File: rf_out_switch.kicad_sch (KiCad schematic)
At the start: 11 parts, among them P15 CONUFL001-SMD-T, P16 CONUFL001-SMD-T, U33 QPC1022TR7, U34 QPC1022TR7

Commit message: Lots of little cleanups
Signed-off-by: Corey Minyard <corey@minyard.net>
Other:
- note added: "Remove this resistor to disable all RF switches, then the zero-ohms connecting TX and RX directly to the antennas can be installed."
- note added: "This RF switch setup handles TX active/standby. On board 1 the zero ohm resistor is not populated. On board 2 or on simplex boards none of the switch circuitry is populated (or the resistor to the left is removed to disable the switches) and only the zero ohm resistor is populated."
- note removed: "This RF switch setup handles TX active/standby. On board 1 the zero ohm resistor is not populated. On board 2 or on simplex boards none of the switch circuitry is populated and only the zero ohm resistor is populated."
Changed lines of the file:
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@@
 		)
 	)
-	(text "This RF switch setup handles TX active/standby.\nOn board 1 the zero ohm resistor is not populated.  On board 2\nor on simplex boards none of the switch circuitry is\npopulated and only the zero ohm resistor is populated."
+	(text "This RF switch setup handles TX active/standby.\nOn board 1 the zero ohm resistor is not populated.  On board 2\nor on simplex boards none of the switch circuitry is\npopulated (or the resistor to the left is removed to disable\nthe switches) and only the zero ohm resistor is populated."
 		(exclude_from_sim no)
 		(at 156.21 147.32 0)
 		(effects
 			(font
+				(size 1.524 1.524)
+			)
+		)
+	)
+	(text "Remove this resistor to disable all RF switches,\nthen the zero-ohms connecting TX and RX directly\nto the antennas can be installed."
+		(exclude_from_sim no)
+		(at 53.848 125.222 0)
+		(effects
+			(font
+				(size 1.524 1.524)
+			)
+		)
+	)
+	(text "Remove this resistor to disable all RF switches,\nthen the zero-ohms connecting TX and RX directly\nto the antennas can be installed."
+		(exclude_from_sim no)
+		(at 53.086 125.222 0)
+		(effects
+			(font

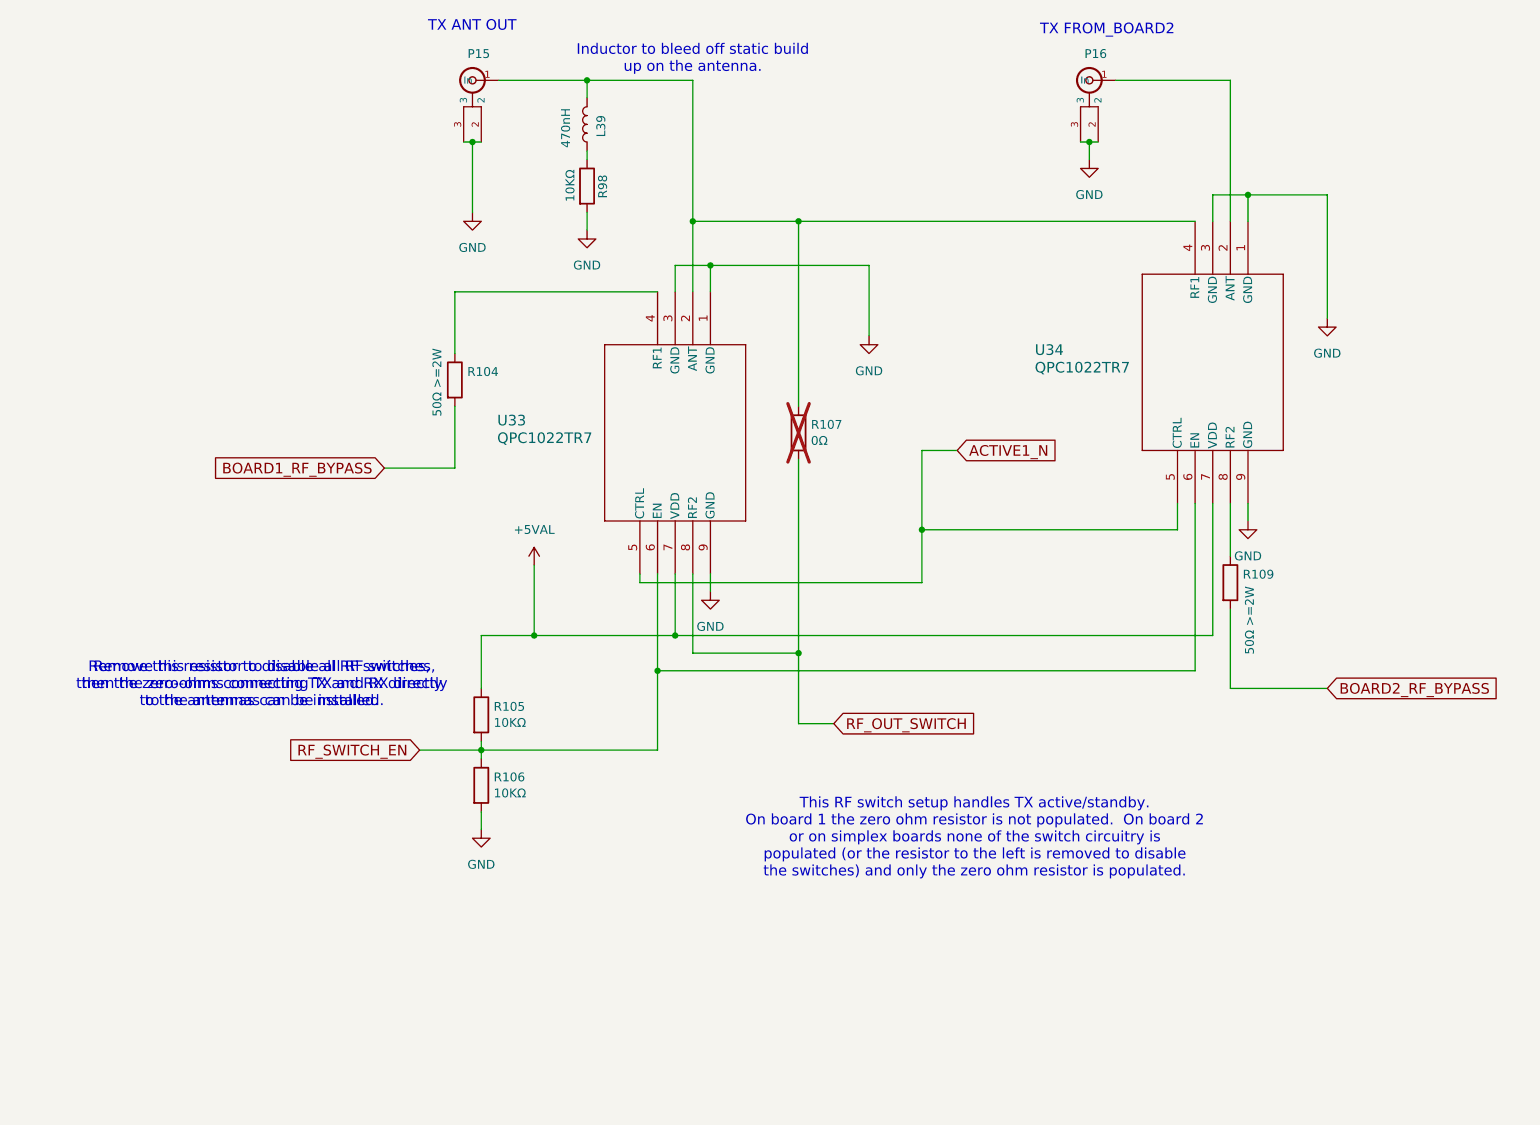
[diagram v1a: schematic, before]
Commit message: Fix a bug in the RF switch circuitry
The board bypass circuitry had an error, the board1 in and antenna
connections were flipped on the switch.  Put them in the right place.

Signed-off-by: Corey Minyard <corey@minyard.net>
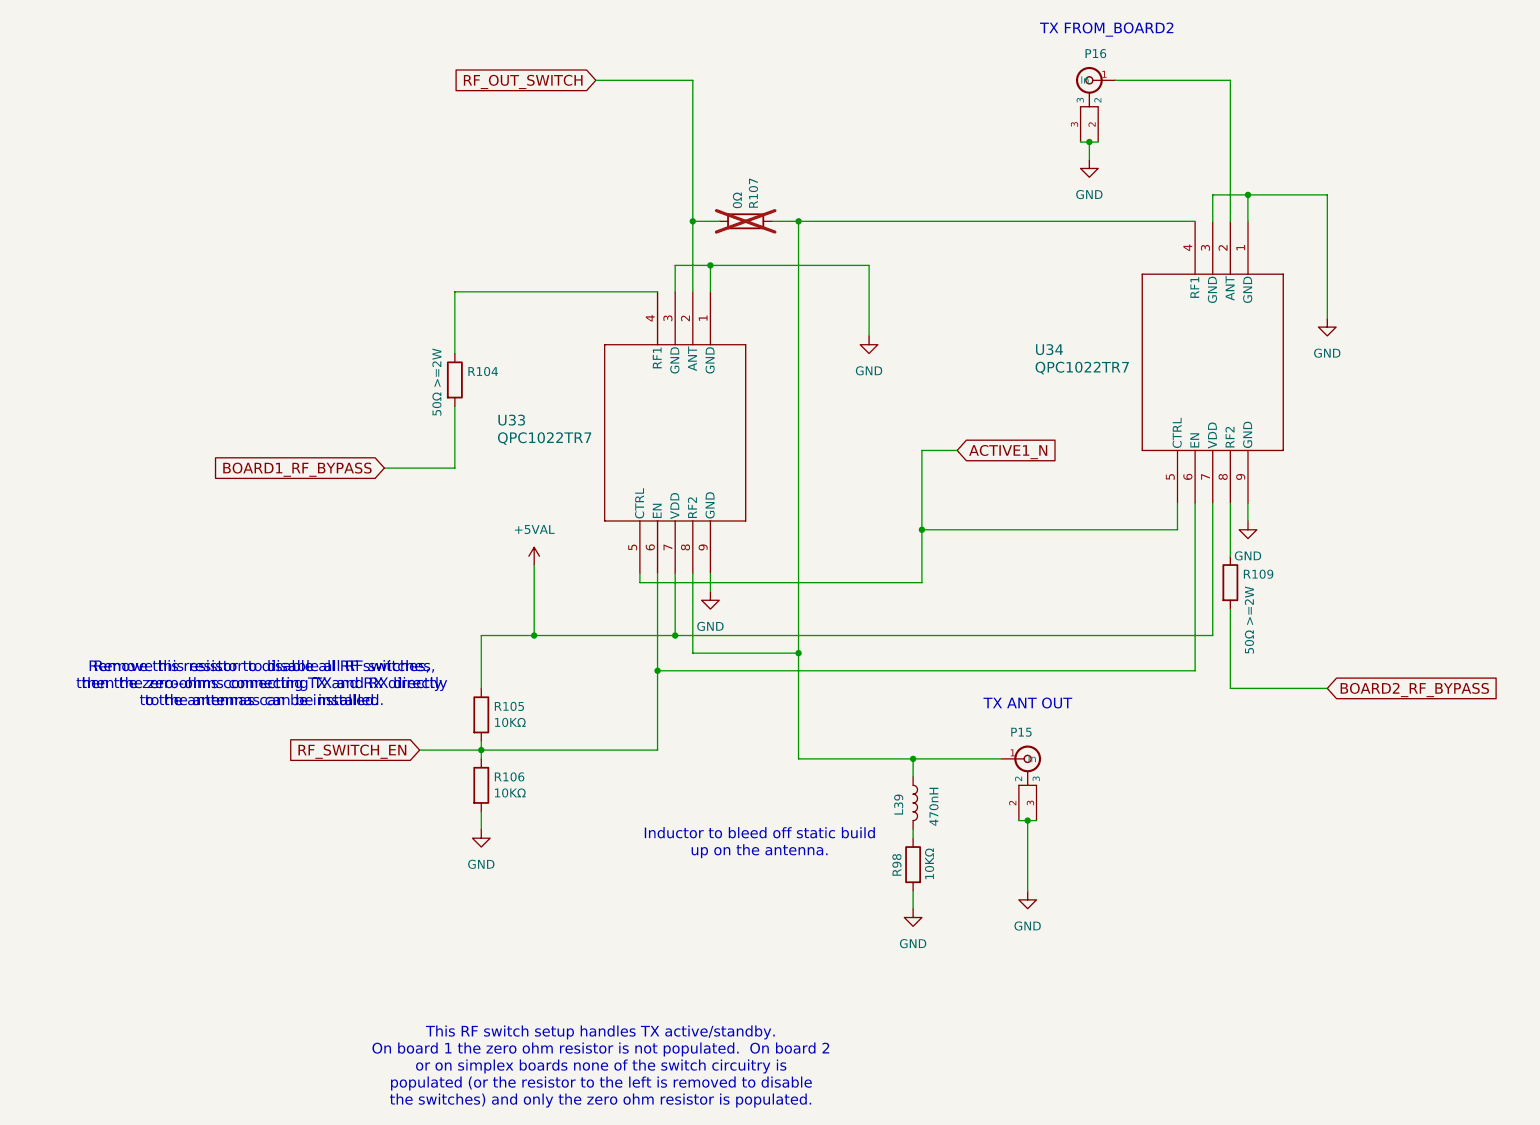
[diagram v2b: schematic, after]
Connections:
- net RF_OUT_SWITCH: now also U33.2 (ANT); no longer U33.8 (RF2)
- net at L39.1, P15.1 (In), R107.1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: now also U33.8 (RF2); no longer U33.2 (ANT)
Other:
- moved on the sheet: L39, P15, R107, R98
